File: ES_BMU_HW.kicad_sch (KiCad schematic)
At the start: 22 parts, among them J1 Conn_02x02_Counter_Clockwise, J2 Conn_02x02_Counter_Clockwise, J3 Conn_02x03_Top_Bottom, J4 Conn_02x06_Top_Bottom, J6 Conn_02x04_Top_Bottom, U1 TPS542025, U7 TLV777

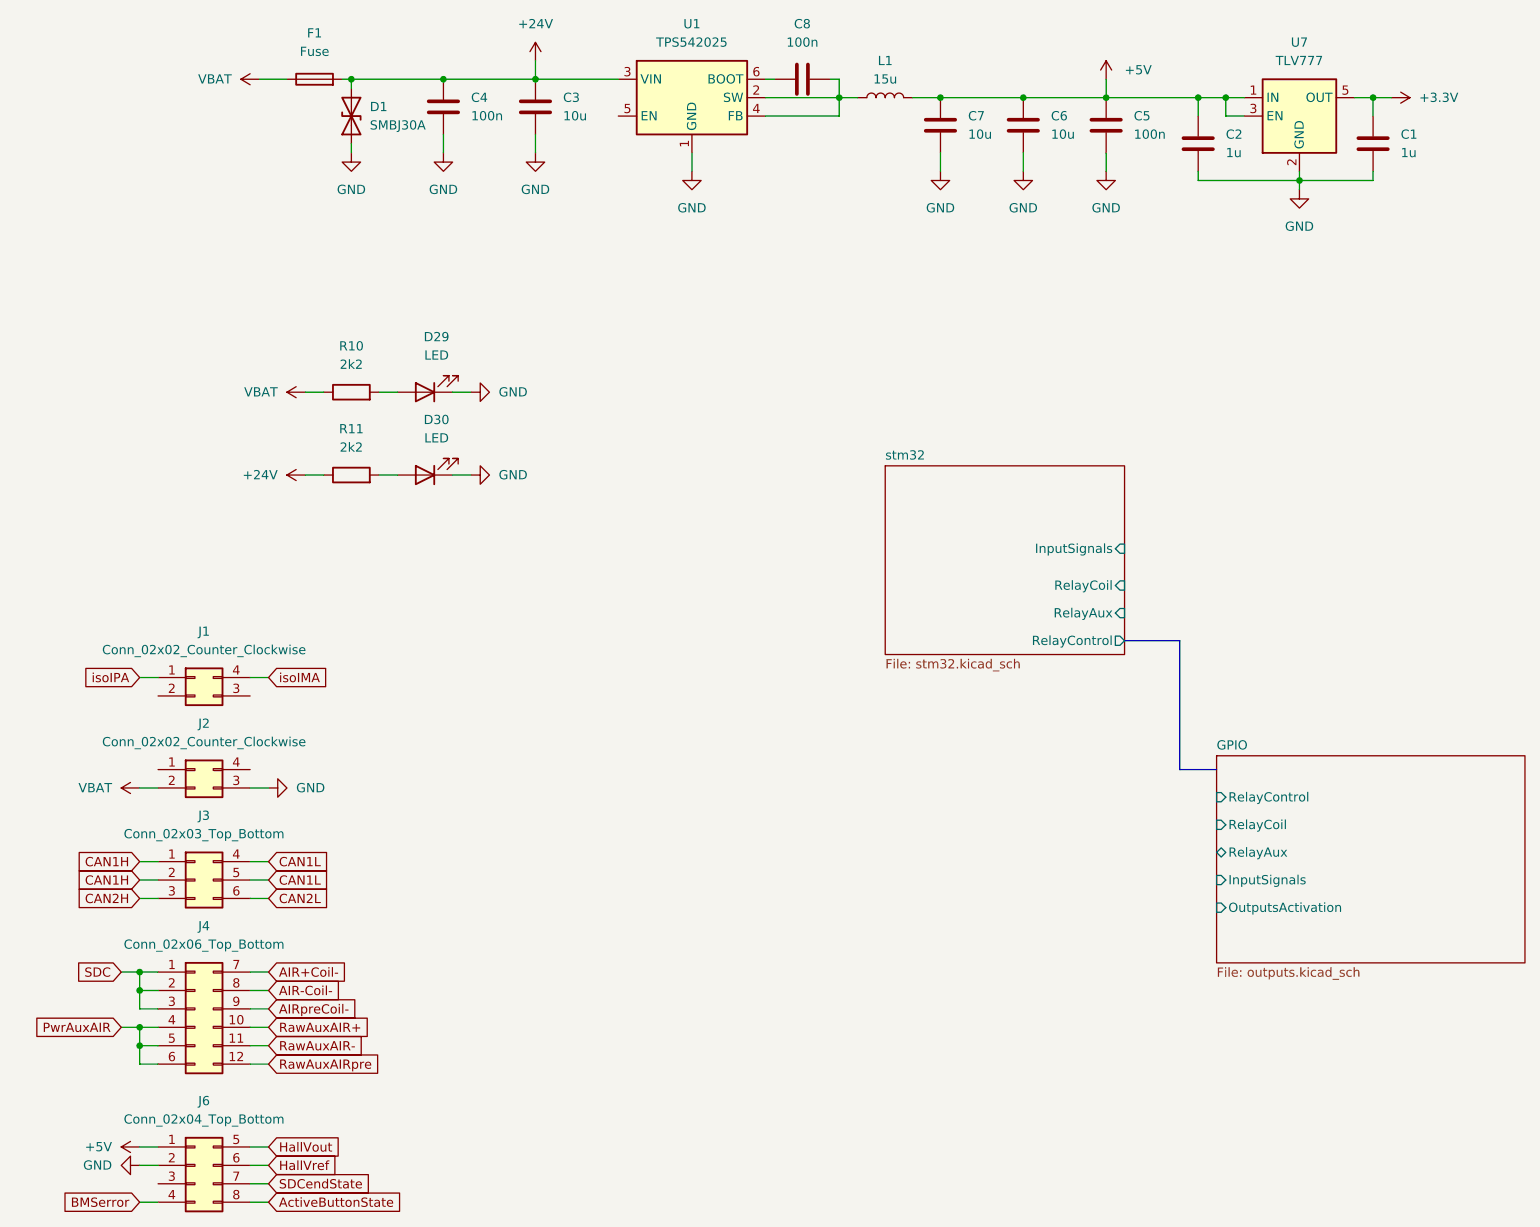
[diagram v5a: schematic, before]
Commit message: Footprints corregides
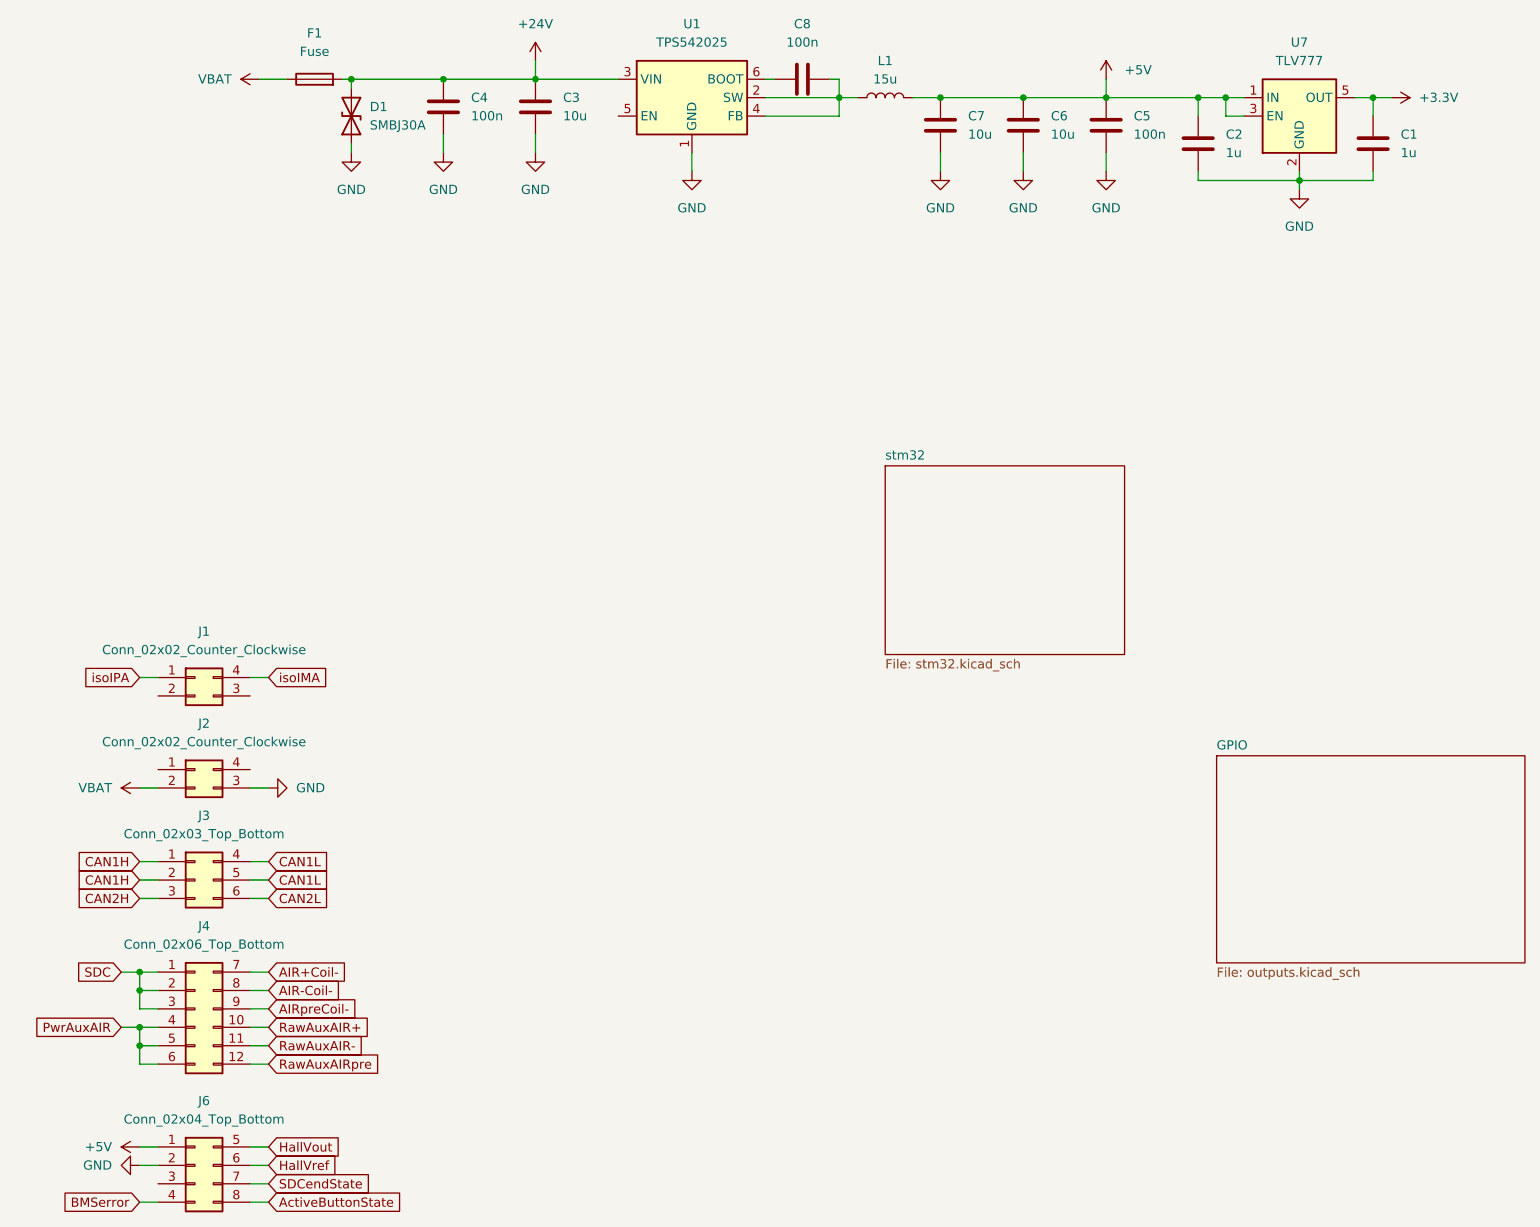
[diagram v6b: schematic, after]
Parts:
- removed D29, D30: LED, symbol Device:LED
- removed R10, R11: 2k2, Resistor_SMD:R_0201_0603Metric_Pad0.64x0.40mm_HandSolder, symbol Device:R
- C1, C2, C3, C4, C5, C6, C7, C8: footprint Capacitor_SMD:C_0603_1608Metric_Pad1.08x0.95mm_HandSolder -> Capacitor_SMD:C_0603_1608Metric
- F1: footprint Fuse:Fuse_1206_3216Metric_Pad1.42x1.75mm_HandSolder -> Fuse:Fuse_1206_3216Metric
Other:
- sheet GPIO ports: added none; removed InputSignals, OutputsActivation, RelayAux, RelayCoil, RelayControl
- sheet stm32 ports: added none; removed InputSignals, RelayAux, RelayCoil, RelayControl

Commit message: - Primer placement dels components - Footprint afegit per la bobina - S'han tret els TVS a les entrades dels contactors auxiliars
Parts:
- L1: footprint (none) -> Inductor_SMD:L_Vishay_IHLP-2020
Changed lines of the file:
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@@
 			)
 		)
-		(property "Footprint" ""
+		(property "Footprint" "Inductor_SMD:L_Vishay_IHLP-2020"
 			(at 142.24 31.75 0)
 			(effects

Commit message: - S'han definit tots els parts numbers de R,C i D ajustant a voltatges i potències - Connectors 02x02 canviats a top2bottom - Modificació de l'error de BMS amb sortida open collector - LED blau afegit per saber l'estat de SDC
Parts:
- removed J1, J2: Conn_02x02_Counter_Clockwise, Connector_Molex:Molex_Nano-Fit_105314-xx04_2x02_P2.50mm_Horizontal, symbol Connector_Generic:Conn_02x02_Counter_Clockwise
- added J1, J2: Conn_02x02_Top_Bottom, Connector_Molex:Molex_Nano-Fit_105314-xx04_2x02_P2.50mm_Horizontal, symbol Connector_Generic:Conn_02x02_Top_Bottom
- C1, C2: Part Number (none) -> VJ0603Y105KXXCW1BC
- C3, C6, C7: footprint Capacitor_SMD:C_0603_1608Metric -> Capacitor_SMD:C_1206_3216Metric; Part Number (none) -> VJ1206G106KXATW1BC
- C4, C5, C8: Part Number (none) -> VJ0603Y104KXACW1BC
- D1: value SMBJ30A -> SMAJ30A; footprint Diode_SMD:D_SMB -> Diode_SMD:D_SMA; symbol Device:D_TVS -> Diode:SMAJ30A; Part Number (none) -> SMAJ30A
- F1: Part Number (none) -> JB12S1001R
- L1: Part Number (none) -> IHLP2020CZER150M01
- U7: Part Number (none) -> TLV77712PDBVR
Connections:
- net +24V: now also D1.1 (A1); no longer D1.2 (A2)
- net GND: now also D1.2 (A2), J2.4 (Pin_4); no longer D1.1 (A1)
- net VBAT: now also J2.2 (Pin_2)
- net isoIMA: now also J1.3 (Pin_3)
- net isoIPA: now also J1.1 (Pin_1)
